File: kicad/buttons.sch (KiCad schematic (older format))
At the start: 11 parts, among them SW1 Left, SW2 Up, SW3 Down, SW4 Right, SW5 Start, SW6 Select, SW7 A, SW8 B

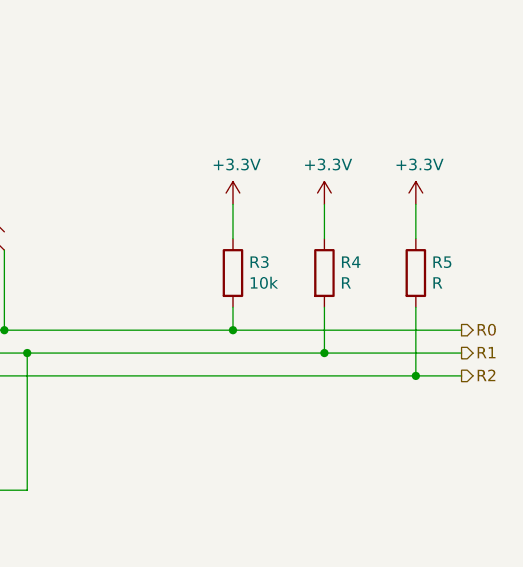
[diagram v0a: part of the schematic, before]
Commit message: Changelog eingeführt, GND statt GNDD
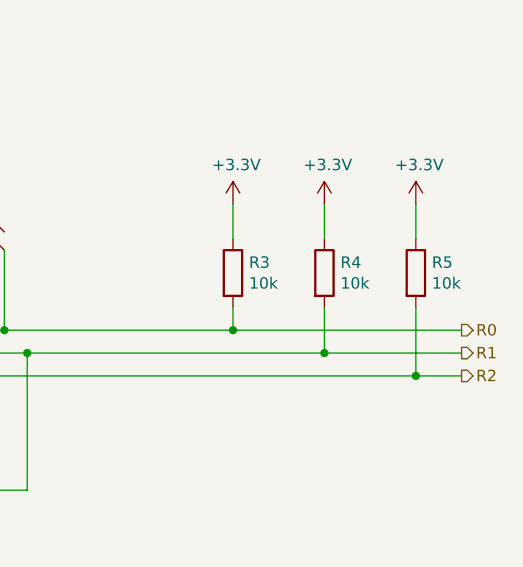
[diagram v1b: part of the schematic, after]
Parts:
- R4, R5: value R -> 10k
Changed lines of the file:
@@
 P 9400 3650
 F 0 "R4" H 9470 3696 50  0000 L CNN
-F 1 "R" H 9470 3605 50  0000 L CNN
+F 1 "10k" H 9470 3605 50  0000 L CNN
 F 2 "Resistor_SMD:R_0603_1608Metric" V 9330 3650 50  0001 C CNN
 F 3 "~" H 9400 3650 50  0001 C CNN
@@
 P 9800 3650
 F 0 "R5" H 9870 3696 50  0000 L CNN
-F 1 "R" H 9870 3605 50  0000 L CNN
+F 1 "10k" H 9870 3605 50  0000 L CNN
 F 2 "Resistor_SMD:R_0603_1608Metric" V 9730 3650 50  0001 C CNN
 F 3 "~" H 9800 3650 50  0001 C CNN

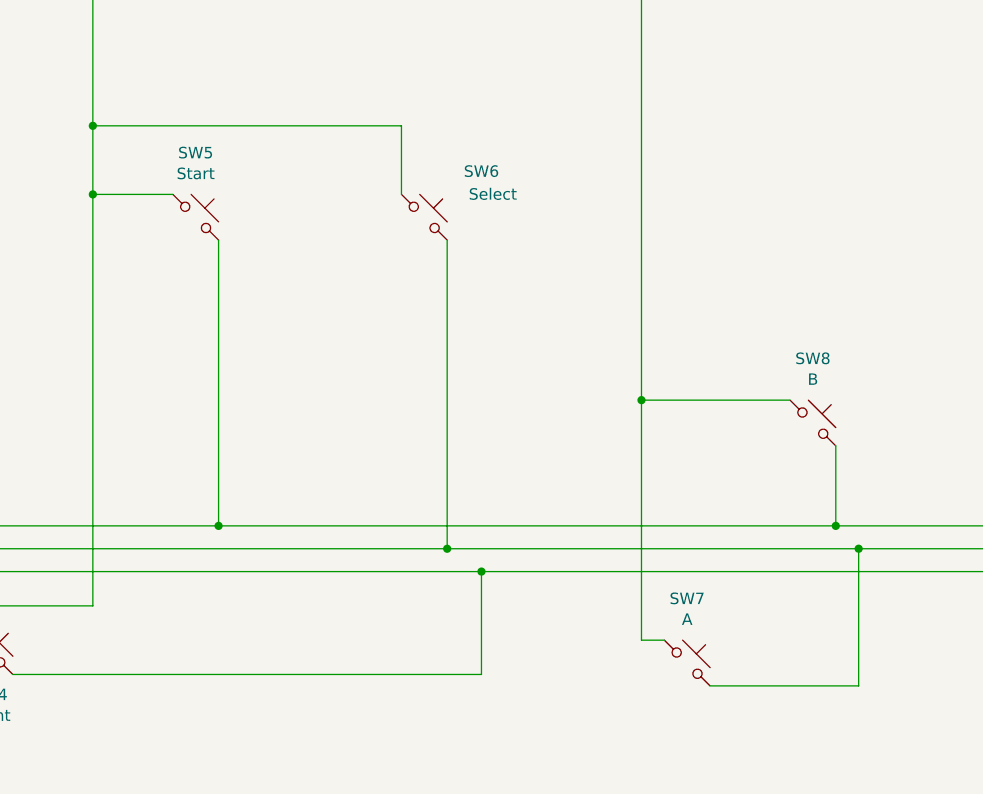
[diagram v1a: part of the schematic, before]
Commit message: Gehäuse updates, Buttons richtig zugewiesen, Tetris
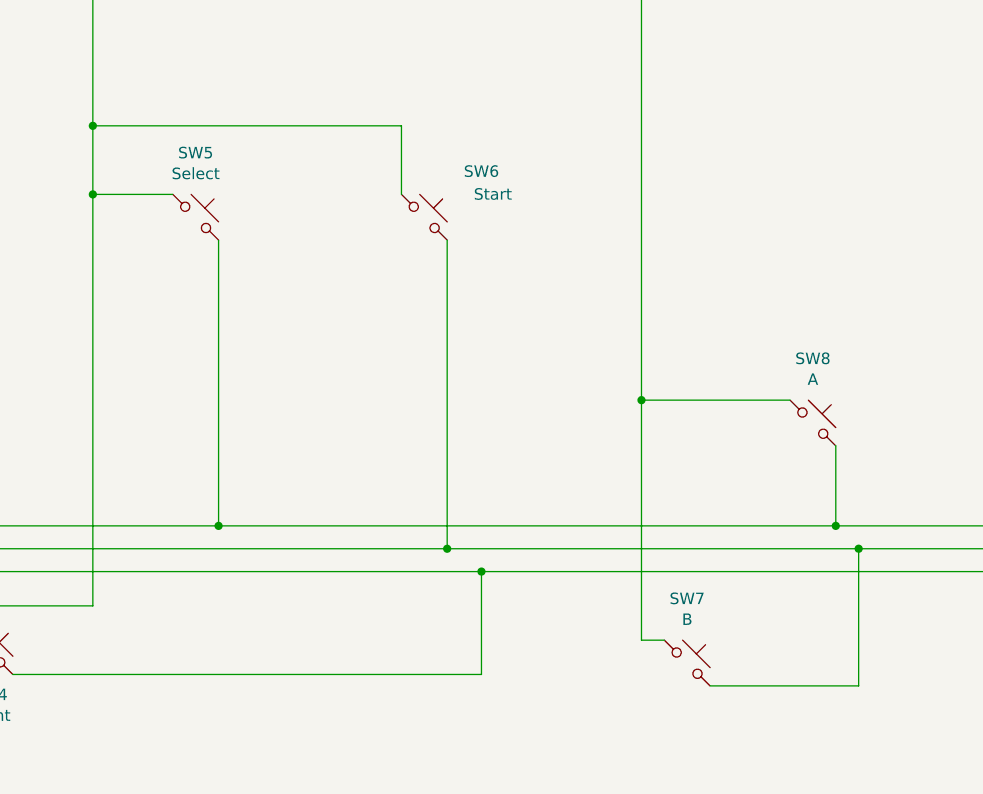
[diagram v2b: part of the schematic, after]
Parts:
- SW5: value Start -> Select
- SW6: value Select -> Start
- SW7: value A -> B
- SW8: value B -> A
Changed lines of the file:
@@
 P 5200 2550
 F 0 "SW5" H 5200 2831 50  0000 C CNN
-F 1 "Start" H 5200 2740 50  0000 C CNN
+F 1 "Select" H 5200 2740 50  0000 C CNN
 F 2 "htl_smd:SW_Push_5.1mm_H1.5mm" H 5200 2750 50  0001 C CNN
 F 3 "~" H 5200 2750 50  0001 C CNN
@@
 P 7350 4500
 F 0 "SW7" H 7350 4781 50  0000 C CNN
-F 1 "A" H 7350 4690 50  0000 C CNN
+F 1 "B" H 7350 4690 50  0000 C CNN
 F 2 "htl_smd:SW_Push_5.1mm_H1.5mm" H 7350 4700 50  0001 C CNN
 F 3 "~" H 7350 4700 50  0001 C CNN
@@
 P 7900 3450
 F 0 "SW8" H 7900 3731 50  0000 C CNN
-F 1 "B" H 7900 3640 50  0000 C CNN
+F 1 "A" H 7900 3640 50  0000 C CNN
 F 2 "htl_smd:SW_Push_5.1mm_H1.5mm" H 7900 3650 50  0001 C CNN
 F 3 "~" H 7900 3650 50  0001 C CNN
@@
 P 6200 2550
 F 0 "SW6" H 6450 2750 50  0000 C CNN
-F 1 "Select" H 6500 2650 50  0000 C CNN
+F 1 "Start" H 6500 2650 50  0000 C CNN
 F 2 "htl_smd:SW_Push_5.1mm_H1.5mm" H 6200 2750 50  0001 C CNN
 F 3 "~" H 6200 2750 50  0001 C CNN

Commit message: Fertiges Layout v0.0.2, 3 Stk bestellt
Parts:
- SW1, SW2, SW3, SW4, SW5, SW6, SW7, SW8: DistOrderNr (none) -> C318884; Distributor (none) -> LCSC; ManPartNr (none) -> TS-1187A-B-A-B; Manufacturer (none) -> XKB Connectivity; Notes (none) -> SMD Taster h=1.2/1.5mm
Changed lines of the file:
@@
 encoding utf-8
 Sheet 2 5
-Title ""
-Date ""
-Rev ""
-Comp ""
-Comment1 ""
-Comment2 ""
+Title "Gamearino"
+Date "2021-04-29"
+Rev "V0.0.2"
+Comp "HTL-Steyr"
+Comment1 "4ABHEL, 2020/2021"
+Comment2 "Hosted by Prof. Karl Zeilhofer"
 Comment3 ""
 Comment4 ""
@@
 F 2 "htl_smd:SW_Push_5.1mm_H1.5mm" H 3500 4000 50  0001 C CNN
 F 3 "~" H 3500 4000 50  0001 C CNN
+F 4 "C318884" H 3500 3800 50  0001 C CNN "DistOrderNr"
+F 5 "LCSC" H 3500 3800 50  0001 C CNN "Distributor"
+F 6 "TS-1187A-B-A-B" H 3500 3800 50  0001 C CNN "ManPartNr"
+F 7 "XKB Connectivity" H 3500 3800 50  0001 C CNN "Manufacturer"
+F 8 "SMD Taster h=1.2/1.5mm" H 3500 3800 50  0001 C CNN "Notes"
 	1    3500 3800
 	1    0    0    -1
@@
 F 2 "htl_smd:SW_Push_5.1mm_H1.5mm" H 2700 4700 50  0001 C CNN
 F 3 "~" H 2700 4700 50  0001 C CNN
+F 4 "C318884" H 2700 4500 50  0001 C CNN "DistOrderNr"
+F 5 "LCSC" H 2700 4500 50  0001 C CNN "Distributor"
+F 6 "TS-1187A-B-A-B" H 2700 4500 50  0001 C CNN "ManPartNr"
+F 7 "XKB Connectivity" H 2700 4500 50  0001 C CNN "Manufacturer"
+F 8 "SMD Taster h=1.2/1.5mm" H 2700 4500 50  0001 C CNN "Notes"
 	1    2700 4500
 	1    0    0    -1
@@
 F 2 "htl_smd:SW_Push_5.1mm_H1.5mm" H 4300 4650 50  0001 C CNN
 F 3 "~" H 4300 4650 50  0001 C CNN
+F 4 "C318884" H 4300 4450 50  0001 C CNN "DistOrderNr"
+F 5 "LCSC" H 4300 4450 50  0001 C CNN "Distributor"
+F 6 "TS-1187A-B-A-B" H 4300 4450 50  0001 C CNN "ManPartNr"
+F 7 "XKB Connectivity" H 4300 4450 50  0001 C CNN "Manufacturer"
+F 8 "SMD Taster h=1.2/1.5mm" H 4300 4450 50  0001 C CNN "Notes"
 	1    4300 4450
 	1    0    0    -1
@@
 F 2 "htl_smd:SW_Push_5.1mm_H1.5mm" H 3550 5650 50  0001 C CNN
 F 3 "~" H 3550 5650 50  0001 C CNN
+F 4 "C318884" H 3550 5450 50  0001 C CNN "DistOrderNr"
+F 5 "LCSC" H 3550 5450 50  0001 C CNN "Distributor"
+F 6 "TS-1187A-B-A-B" H 3550 5450 50  0001 C CNN "ManPartNr"
+F 7 "XKB Connectivity" H 3550 5450 50  0001 C CNN "Manufacturer"
+F 8 "SMD Taster h=1.2/1.5mm" H 3550 5450 50  0001 C CNN "Notes"
 	1    3550 5450
 	1    0    0    -1
@@
 AR Path="/5F8674B3/603D5276" Ref="#PWR?"  Part="1"
 AR Path="/603D5276" Ref="#PWR?"  Part="1"
-AR Path="/603CE165/603D5276" Ref="#PWR03"  Part="1"
-F 0 "#PWR03" H 9000 3200 50  0001 C CNN
+AR Path="/603CE165/603D5276" Ref="#PWR05"  Part="1"
+F 0 "#PWR05" H 9000 3200 50  0001 C CNN
 F 1 "+3.3V" H 9015 3523 50  0000 C CNN
 F 2 "" H 9000 3350 50  0001 C CNN
@@
 F 2 "htl_smd:SW_Push_5.1mm_H1.5mm" H 5200 2750 50  0001 C CNN
 F 3 "~" H 5200 2750 50  0001 C CNN
+F 4 "C318884" H 5200 2550 50  0001 C CNN "DistOrderNr"
+F 5 "LCSC" H 5200 2550 50  0001 C CNN "Distributor"
+F 6 "TS-1187A-B-A-B" H 5200 2550 50  0001 C CNN "ManPartNr"
+F 7 "XKB Connectivity" H 5200 2550 50  0001 C CNN "Manufacturer"
+F 8 "SMD Taster h=1.2/1.5mm" H 5200 2550 50  0001 C CNN "Notes"
 	1    5200 2550
 	1    0    0    -1
@@
 F 2 "htl_smd:SW_Push_5.1mm_H1.5mm" H 7350 4700 50  0001 C CNN
 F 3 "~" H 7350 4700 50  0001 C CNN
+F 4 "C318884" H 7350 4500 50  0001 C CNN "DistOrderNr"
+F 5 "LCSC" H 7350 4500 50  0001 C CNN "Distributor"
+F 6 "TS-1187A-B-A-B" H 7350 4500 50  0001 C CNN "ManPartNr"
+F 7 "XKB Connectivity" H 7350 4500 50  0001 C CNN "Manufacturer"
+F 8 "SMD Taster h=1.2/1.5mm" H 7350 4500 50  0001 C CNN "Notes"
 	1    7350 4500
 	1    0    0    -1
@@
 AR Path="/5F8674B3/603D6F16" Ref="#PWR?"  Part="1"
 AR Path="/603D6F16" Ref="#PWR?"  Part="1"
-AR Path="/603CE165/603D6F16" Ref="#PWR04"  Part="1"
-F 0 "#PWR04" H 9400 3200 50  0001 C CNN
+AR Path="/603CE165/603D6F16" Ref="#PWR06"  Part="1"
+F 0 "#PWR06" H 9400 3200 50  0001 C CNN
 F 1 "+3.3V" H 9415 3523 50  0000 C CNN
 F 2 "" H 9400 3350 50  0001 C CNN
@@
 F 2 "htl_smd:SW_Push_5.1mm_H1.5mm" H 7900 3650 50  0001 C CNN
 F 3 "~" H 7900 3650 50  0001 C CNN
+F 4 "C318884" H 7900 3450 50  0001 C CNN "DistOrderNr"
+F 5 "LCSC" H 7900 3450 50  0001 C CNN "Distributor"
+F 6 "TS-1187A-B-A-B" H 7900 3450 50  0001 C CNN "ManPartNr"
+F 7 "XKB Connectivity" H 7900 3450 50  0001 C CNN "Manufacturer"
+F 8 "SMD Taster h=1.2/1.5mm" H 7900 3450 50  0001 C CNN "Notes"
 	1    7900 3450
 	1    0    0    -1
@@
 AR Path="/5F8674B3/603D7C4D" Ref="#PWR?"  Part="1"
 AR Path="/603D7C4D" Ref="#PWR?"  Part="1"
-AR Path="/603CE165/603D7C4D" Ref="#PWR05"  Part="1"
-F 0 "#PWR05" H 9800 3200 50  0001 C CNN
+AR Path="/603CE165/603D7C4D" Ref="#PWR07"  Part="1"
+F 0 "#PWR07" H 9800 3200 50  0001 C CNN
 F 1 "+3.3V" H 9815 3523 50  0000 C CNN
 F 2 "" H 9800 3350 50  0001 C CNN
@@
 F 2 "htl_smd:SW_Push_5.1mm_H1.5mm" H 6200 2750 50  0001 C CNN
 F 3 "~" H 6200 2750 50  0001 C CNN
+F 4 "C318884" H 6200 2550 50  0001 C CNN "DistOrderNr"
+F 5 "LCSC" H 6200 2550 50  0001 C CNN "Distributor"
+F 6 "TS-1187A-B-A-B" H 6200 2550 50  0001 C CNN "ManPartNr"
+F 7 "XKB Connectivity" H 6200 2550 50  0001 C CNN "Manufacturer"
+F 8 "SMD Taster h=1.2/1.5mm" H 6200 2550 50  0001 C CNN "Notes"
 	1    6200 2550
 	1    0    0    -1

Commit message: BOM fertig eingepflegt
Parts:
- R3, R4, R5: DistOrderNr (none) -> C103210; Distributor (none) -> LCSC; ManPartNr (none) -> RTT03103JTP; Manufacturer (none) -> RALEC; Notes (none) -> 10kΩ ±5% 0.1W ±100ppm/℃; PriceEUR (none) -> 0.0015; PriceForQty (none) -> 100
- SW1, SW2, SW3, SW4, SW5, SW6, SW7, SW8: PriceEUR (none) -> 0.0129; PriceForQty (none) -> 50
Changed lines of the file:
@@
 F 7 "XKB Connectivity" H 3500 3800 50  0001 C CNN "Manufacturer"
 F 8 "SMD Taster h=1.2/1.5mm" H 3500 3800 50  0001 C CNN "Notes"
+F 9 "0.0129" H 3500 3800 50  0001 C CNN "PriceEUR"
+F 10 "50" H 3500 3800 50  0001 C CNN "PriceForQty"
 	1    3500 3800
 	1    0    0    -1
@@
 F 7 "XKB Connectivity" H 2700 4500 50  0001 C CNN "Manufacturer"
 F 8 "SMD Taster h=1.2/1.5mm" H 2700 4500 50  0001 C CNN "Notes"
+F 9 "0.0129" H 2700 4500 50  0001 C CNN "PriceEUR"
+F 10 "50" H 2700 4500 50  0001 C CNN "PriceForQty"
 	1    2700 4500
 	1    0    0    -1
@@
 F 7 "XKB Connectivity" H 4300 4450 50  0001 C CNN "Manufacturer"
 F 8 "SMD Taster h=1.2/1.5mm" H 4300 4450 50  0001 C CNN "Notes"
+F 9 "0.0129" H 4300 4450 50  0001 C CNN "PriceEUR"
+F 10 "50" H 4300 4450 50  0001 C CNN "PriceForQty"
 	1    4300 4450
 	1    0    0    -1
@@
 F 7 "XKB Connectivity" H 3550 5450 50  0001 C CNN "Manufacturer"
 F 8 "SMD Taster h=1.2/1.5mm" H 3550 5450 50  0001 C CNN "Notes"
+F 9 "0.0129" H 3550 5450 50  0001 C CNN "PriceEUR"
+F 10 "50" H 3550 5450 50  0001 C CNN "PriceForQty"
 	1    3550 5450
 	1    0    0    -1
@@
 F 2 "Resistor_SMD:R_0603_1608Metric" V 8930 3650 50  0001 C CNN
 F 3 "~" H 9000 3650 50  0001 C CNN
+F 4 "C103210" H 9000 3650 50  0001 C CNN "DistOrderNr"
+F 5 "LCSC" H 9000 3650 50  0001 C CNN "Distributor"
+F 6 "RTT03103JTP" H 9000 3650 50  0001 C CNN "ManPartNr"
+F 7 "RALEC" H 9000 3650 50  0001 C CNN "Manufacturer"
+F 8 "10kΩ ±5% 0.1W ±100ppm/℃" H 9000 3650 50  0001 C CNN "Notes"
+F 9 "0.0015" H 9000 3650 50  0001 C CNN "PriceEUR"
+F 10 "100" H 9000 3650 50  0001 C CNN "PriceForQty"
 	1    9000 3650
 	1    0    0    -1
@@
 F 7 "XKB Connectivity" H 5200 2550 50  0001 C CNN "Manufacturer"
 F 8 "SMD Taster h=1.2/1.5mm" H 5200 2550 50  0001 C CNN "Notes"
+F 9 "0.0129" H 5200 2550 50  0001 C CNN "PriceEUR"
+F 10 "50" H 5200 2550 50  0001 C CNN "PriceForQty"
 	1    5200 2550
 	1    0    0    -1
@@
 F 7 "XKB Connectivity" H 7350 4500 50  0001 C CNN "Manufacturer"
 F 8 "SMD Taster h=1.2/1.5mm" H 7350 4500 50  0001 C CNN "Notes"
+F 9 "0.0129" H 7350 4500 50  0001 C CNN "PriceEUR"
+F 10 "50" H 7350 4500 50  0001 C CNN "PriceForQty"
 	1    7350 4500
 	1    0    0    -1
@@
 F 2 "Resistor_SMD:R_0603_1608Metric" V 9330 3650 50  0001 C CNN
 F 3 "~" H 9400 3650 50  0001 C CNN
+F 4 "C103210" H 9400 3650 50  0001 C CNN "DistOrderNr"
+F 5 "LCSC" H 9400 3650 50  0001 C CNN "Distributor"
+F 6 "RTT03103JTP" H 9400 3650 50  0001 C CNN "ManPartNr"
+F 7 "RALEC" H 9400 3650 50  0001 C CNN "Manufacturer"
+F 8 "10kΩ ±5% 0.1W ±100ppm/℃" H 9400 3650 50  0001 C CNN "Notes"
+F 9 "0.0015" H 9400 3650 50  0001 C CNN "PriceEUR"
+F 10 "100" H 9400 3650 50  0001 C CNN "PriceForQty"
 	1    9400 3650
 	1    0    0    -1
@@
 F 7 "XKB Connectivity" H 7900 3450 50  0001 C CNN "Manufacturer"
 F 8 "SMD Taster h=1.2/1.5mm" H 7900 3450 50  0001 C CNN "Notes"
+F 9 "0.0129" H 7900 3450 50  0001 C CNN "PriceEUR"
+F 10 "50" H 7900 3450 50  0001 C CNN "PriceForQty"
 	1    7900 3450
 	1    0    0    -1
@@
 F 2 "Resistor_SMD:R_0603_1608Metric" V 9730 3650 50  0001 C CNN
 F 3 "~" H 9800 3650 50  0001 C CNN
+F 4 "C103210" H 9800 3650 50  0001 C CNN "DistOrderNr"
+F 5 "LCSC" H 9800 3650 50  0001 C CNN "Distributor"
+F 6 "RTT03103JTP" H 9800 3650 50  0001 C CNN "ManPartNr"
+F 7 "RALEC" H 9800 3650 50  0001 C CNN "Manufacturer"
+F 8 "10kΩ ±5% 0.1W ±100ppm/℃" H 9800 3650 50  0001 C CNN "Notes"
+F 9 "0.0015" H 9800 3650 50  0001 C CNN "PriceEUR"
+F 10 "100" H 9800 3650 50  0001 C CNN "PriceForQty"
 	1    9800 3650
 	1    0    0    -1
@@
 F 7 "XKB Connectivity" H 6200 2550 50  0001 C CNN "Manufacturer"
 F 8 "SMD Taster h=1.2/1.5mm" H 6200 2550 50  0001 C CNN "Notes"
+F 9 "0.0129" H 6200 2550 50  0001 C CNN "PriceEUR"
+F 10 "50" H 6200 2550 50  0001 C CNN "PriceForQty"
 	1    6200 2550
 	1    0    0    -1
